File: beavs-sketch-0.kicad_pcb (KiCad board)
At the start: 4 copper layers, 50 x 70 mm, 136 parts, among them J1 USB_C_Receptacle_USB2.0_16P, J10 Conn_01x03, J11 Conn_01x03, J12 Micro_SD_Card, J13 Conn_02x02_Odd_Even, J2 Conn_Coaxial, J3 Conn_01x02, J4 Conn_Coaxial, J5 Conn_01x02, J6 Conn_01x03, J7 Conn_01x03, J8 Conn_01x03, J9 Conn_01x03, Q1 CSD17575Q3, Q2 CSD17575Q3, SW1 SW_Push, SW2 SW_Push, U1 RP2040, U10 INA745A, U11 INA745A, U12 INA745A, U13 INA745A, U14 ISM6HG256X, U15 SN74LVC4245APW, U16 SRV05-4, U17 SRV05-4, U18 LIS2MDL, U19 LM74502, U2 W25Q128JVS, U3 MS5607-02BA, U4 RFM95W-915S2, U5 MAX-M10S, U6 INA745A, U7 AMS1117-3.3, U8 AMS1117-5.0, U9 INA745A, Y1 Crystal_GND24

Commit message: add reset pullup...
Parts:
- added R14: 5.1k, Resistor_SMD:R_0402_1005Metric, F.Cu at (224.8, 63.4)
- moved SW1 0.90 mm to (225.3, 66.9)
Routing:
- net +3V3: track 58.7 -> 59.3 mm, vias 30 -> 31
- net GND: vias 288 -> 290

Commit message: various tweaks
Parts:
- added TP1: TestPoint, TestPoint:TestPoint_Pad_D1.0mm, B.Cu at (209.9, 95.2)
- added TP2: TestPoint, TestPoint:TestPoint_Pad_D1.0mm, B.Cu at (212.2, 95.3)
- R11: value 120 -> 1k
- moved C3 15.7 mm to (215.1, 96.5)
- moved J1 0.32 mm to (223.2, 82.5)
- moved C16 0.06 mm to (192.3, 122.0)
- turned R11 to -90 degrees
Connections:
- R11 pad 1: Net-(U5-TIMEPULSE) -> Net-(D10-A)
- R11 pad 2: Net-(D10-A) -> Net-(U5-TIMEPULSE)
- U1 pad 19: unconnected-(U1-TESTEN-Pad19) -> GND
- U1 pad 24: unconnected-(U1-SWCLK-Pad24) -> Net-(U1-SWCLK)
- U1 pad 25: unconnected-(U1-SWD-Pad25) -> Net-(U1-SWD)
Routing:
- net +3V3: track 59.3 -> 50.7 mm, vias 31 -> 32
- net Net-(U1-SWCLK): track 0.00 -> 3.81 mm, vias 0 -> 1
- net Net-(U1-SWD): track 0.00 -> 3.33 mm, vias 0 -> 1
- net GND: track 34.3 -> 35.5 mm, vias 290 -> 305
- net unconnected-(U1-SWD-Pad25): track 1.16 -> 0.00 mm, vias 1 -> 0
- net unconnected-(U1-SWCLK-Pad24): track 1.07 -> 0.00 mm, vias 1 -> 0

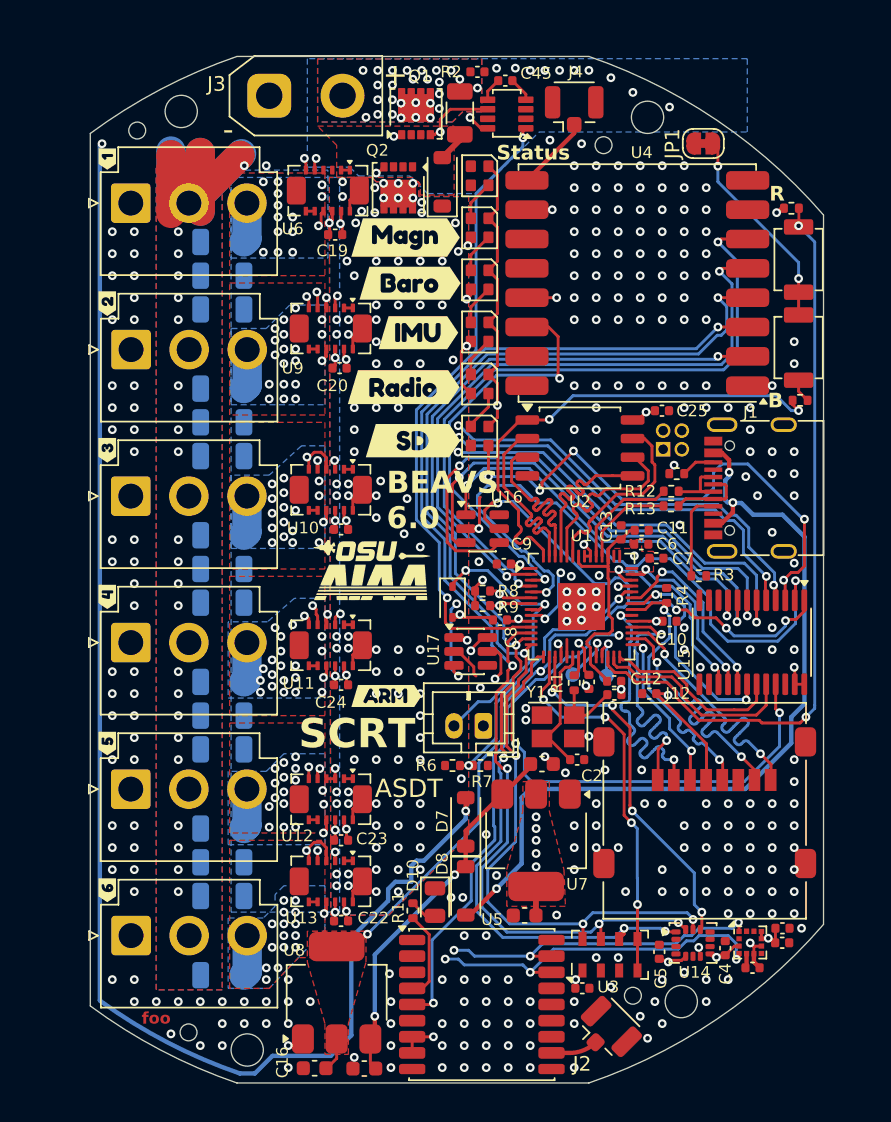
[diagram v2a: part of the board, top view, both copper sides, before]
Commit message: fix pin order on FETs, cleanup
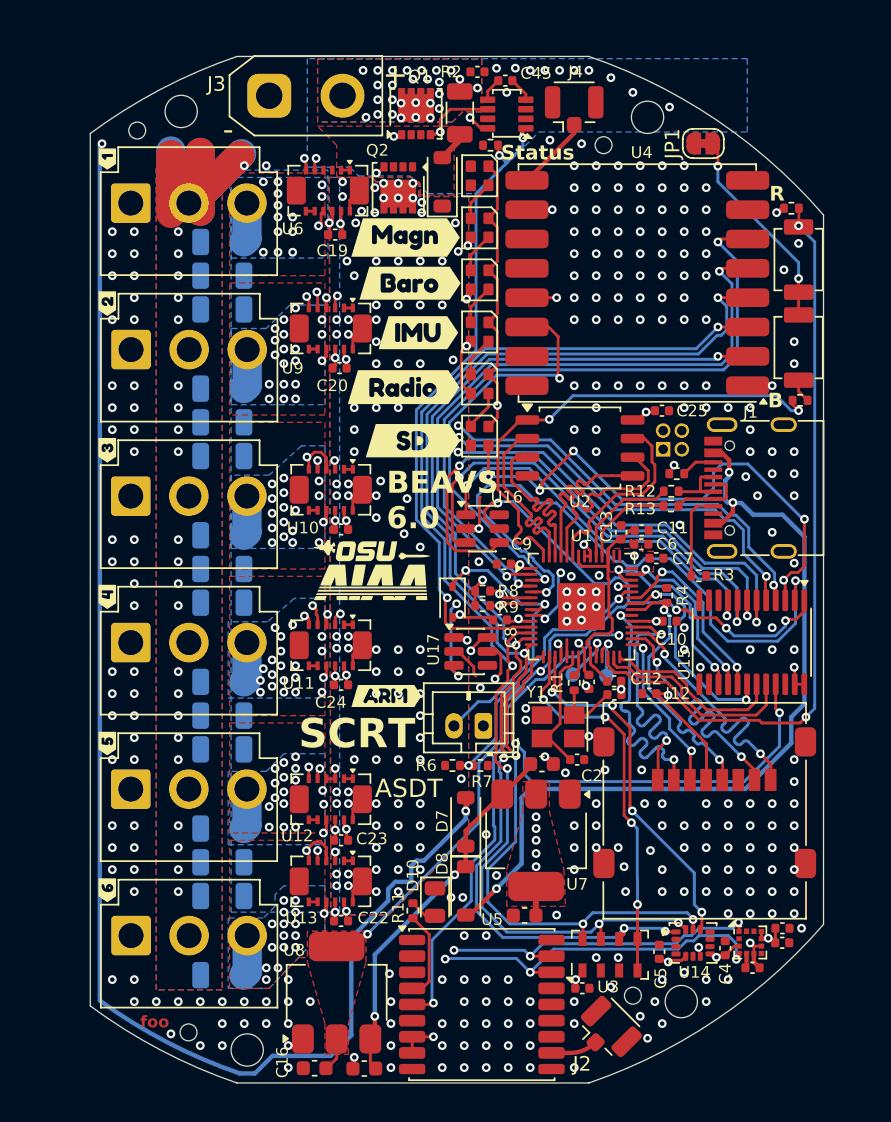
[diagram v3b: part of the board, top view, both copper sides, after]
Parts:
- added R15: 5.1k, Resistor_SMD:R_0402_1005Metric, F.Cu at (204.3, 59.1)
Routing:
- net /Power/EN: track 43.8 -> 45.2 mm, vias 2 -> 3
- net GND: vias 305 -> 311

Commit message: switching to electrolytic caps
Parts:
- removed C31, C32, C33, C34, C35, C36, C37, C38, C39, C40, C41, C42, C43, C44: 47u, Capacitor_SMD:C_1206_3216Metric
- C27, C30: value 47u -> 220u; footprint Capacitor_SMD:C_1206_3216Metric -> Capacitor_THT:CP_Radial_D5.0mm_P2.00mm; moved to F.Cu
- moved C27 14.4 mm to (193.9, 77.8)
- moved C30 11.8 mm to (193.8, 66.9)
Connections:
- C27 pad 1: Net-(J6-Pin_3) -> +BATT
- C30 pad 1: Net-(J7-Pin_3) -> +BATT
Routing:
- net SCL: track 113.8 -> 116.2 mm
- net SDA: track 113.6 -> 115.6 mm
- net Net-(J7-Pin_3): vias 18 -> 17
- net Net-(J6-Pin_3): vias 13 -> 12
- net +BATT: vias 90 -> 89
